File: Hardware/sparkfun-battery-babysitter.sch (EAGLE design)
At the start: 55 parts, among them U1 BQ24075, U2 BQ27441-G1

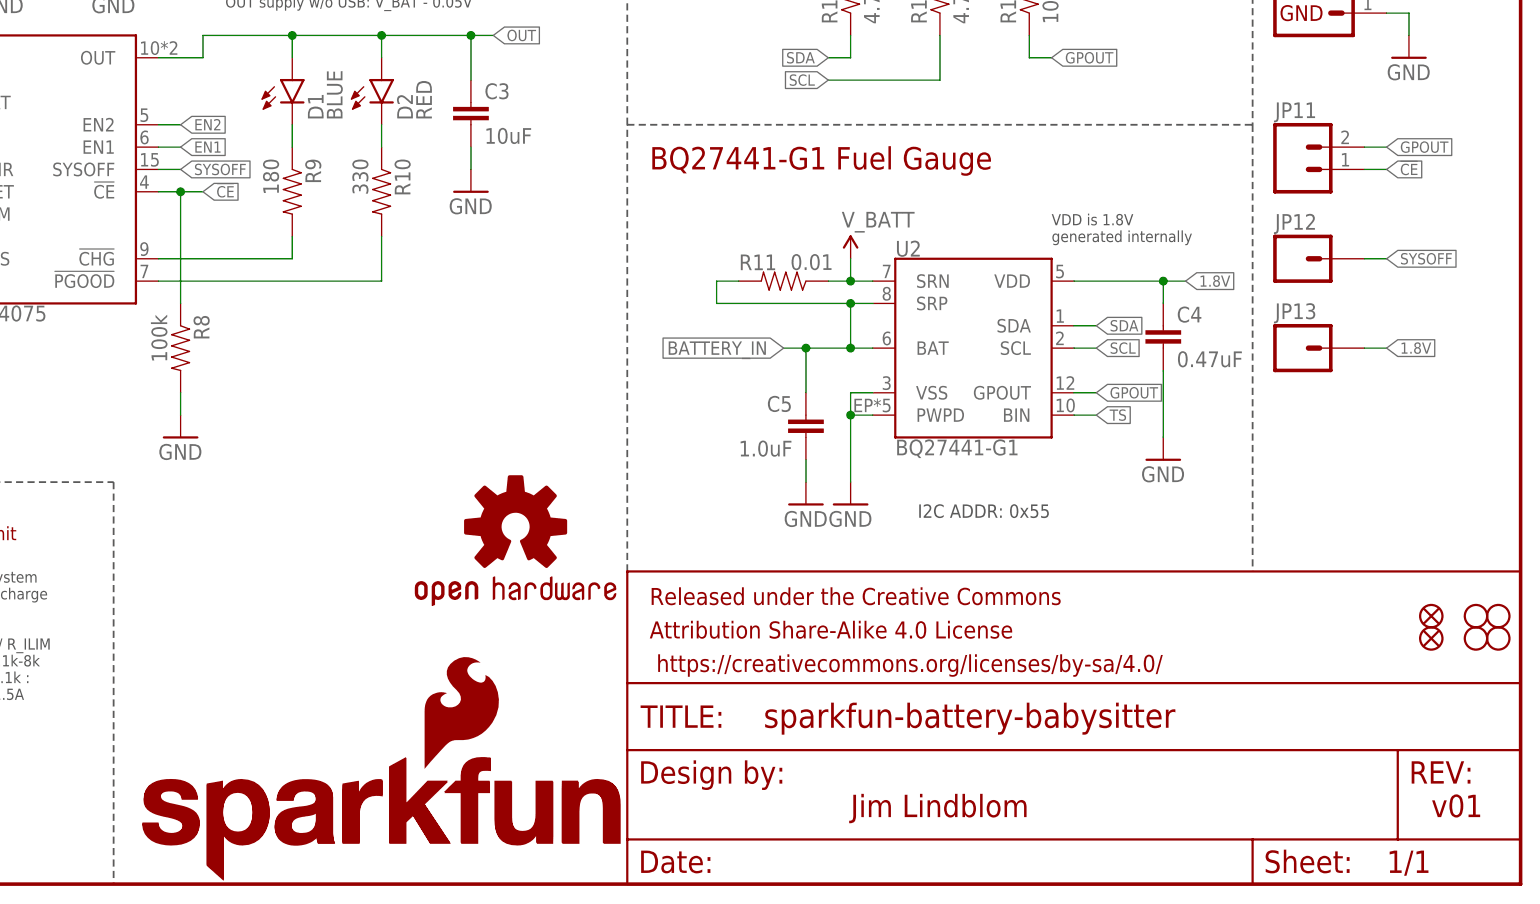
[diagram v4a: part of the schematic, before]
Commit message: Adding SJ5, to set power LED to PWR or PGOOD.
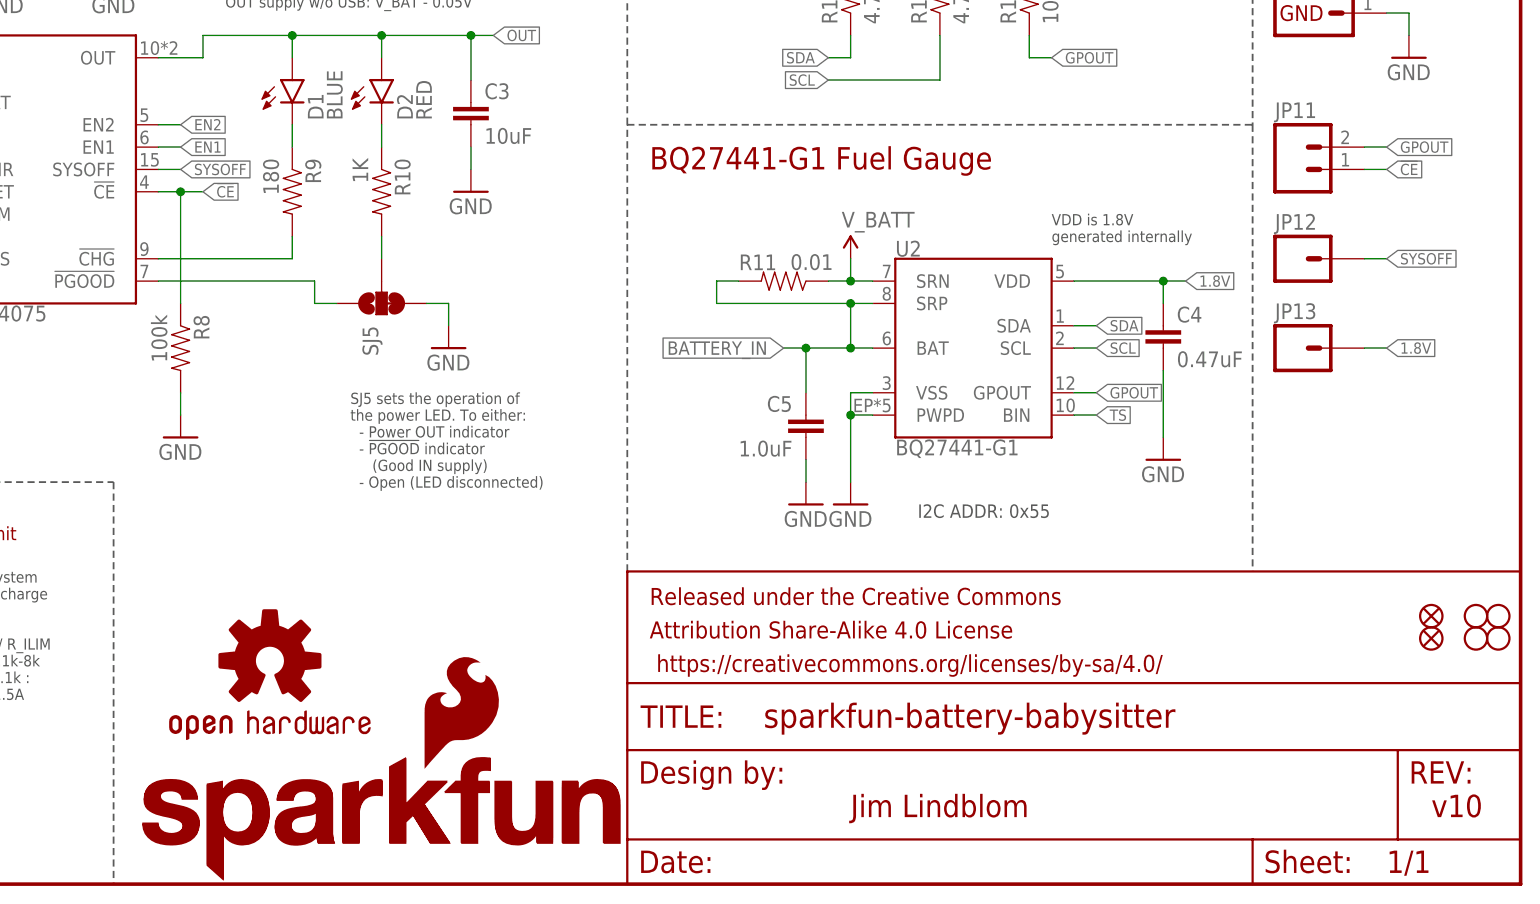
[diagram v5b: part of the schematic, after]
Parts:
- added SJ5: JUMPER-PAD-3-2OF3_NC_BY_TRACE_SMALL, SparkFun-Passives:JUMPER-PAD-3-2OF3_NC_BY_TRACE_SMALL
- R10: value 330 -> 1K; device SparkFun-Resistors:330OHM1/10W1%(0603) -> SparkFun-Resistors:1KOHM-1/10W-1%(0603)
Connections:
- new net N$5: R10.2, SJ5.2
- net !PGOOD!: now also SJ5.1; no longer R10.2
- net GND: now also SJ5.3
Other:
- note added: "SJ5 sets the operation of the power LED. To either: - Power OUT indicator - !PGOOD! indicator (Good IN supply) - Open (LED disconnected)"
- note added: "v10"
- note removed: "v01"
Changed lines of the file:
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@@
 <?xml version="1.0" encoding="utf-8"?>
 <!DOCTYPE eagle SYSTEM "eagle.dtd">
-<eagle version="7.1.0">
+<eagle version="7.5.0">
 <drawing>
 <settings>
@@
 <part name="D2" library="SparkFun-LED" deviceset="LED-RED" device="0603" value="RED"/>
 <part name="R9" library="SparkFun-Resistors" deviceset="180OHM1/10W1%(0603)" device="" value="180"/>
-<part name="R10" library="SparkFun-Resistors" deviceset="330OHM1/10W1%(0603)" device="" value="330"/>
+<part name="R10" library="SparkFun-Resistors" deviceset="1KOHM-1/10W-1%(0603)" device="" value="1K"/>
 <part name="C3" library="SparkFun-Capacitors" deviceset="10UF10V10%(0805)" device="" value="10uF"/>
 <part name="GND15" library="SparkFun-Aesthetics" deviceset="GND" device=""/>
@@
 <attribute name="PROD_ID" value="SWCH-13215"/>
 </part>
+<part name="GND24" library="SparkFun-Aesthetics" deviceset="GND" device=""/>
+<part name="SJ5" library="SparkFun-Passives" deviceset="JUMPER-PAD-3-2OF3_NC_BY_TRACE" device="_SMALL" value=""/>
 </parts>
 <sheets>
@@
 <text x="220.98" y="127" size="2.54" layer="94" align="top-left">Headers</text>
 <text x="172.72" y="10.16" size="2.54" layer="94" align="top-left">Jim Lindblom</text>
-<text x="238.76" y="10.16" size="2.54" layer="94" align="top-left">v01</text>
+<text x="238.76" y="10.16" size="2.54" layer="94" align="top-left">v10</text>
 <text x="149.86" y="152.4" size="1.27" layer="97">SYSOFF controls supply
 to the V_OUT pin.
@@
 OUT supply w/o USB: V_BAT - 0.05V</text>
 <text x="180.34" y="43.18" size="1.524" layer="97" align="top-left">I2C ADDR: 0x55</text>
+<text x="115.824" y="55.88" size="1.27" layer="97" align="top-left">SJ5 sets the operation of
+the power LED. To either:
+  - Power OUT indicator
+  - !PGOOD! indicator
+     (Good IN supply)
+  - Open (LED disconnected)</text>
 </plain>
 <instances>
@@
 <instance part="JP4" gate="G$1" x="43.18" y="147.32"/>
 <instance part="LOGO1" gate="G$1" x="90.17" y="0.508"/>
-<instance part="LOGO3" gate="G$1" x="134.62" y="40.64"/>
+<instance part="LOGO3" gate="G$1" x="106.68" y="25.4"/>
 <instance part="R12" gate="G$1" x="177.8" y="157.48" rot="R270"/>
 <instance part="JP11" gate="G$1" x="223.52" y="81.28"/>
@@
 <attribute name="PROD_ID" x="231.14" y="149.86" size="1.27" layer="96" rot="R270" display="off"/>
 </instance>
+<instance part="GND24" gate="1" x="127" y="60.96"/>
+<instance part="SJ5" gate="G$1" x="119.38" y="66.04" rot="MR270"/>
 </instances>
 <busses>
@@
 <wire x1="27.94" y1="66.04" x2="27.94" y2="68.58" width="0.1524" layer="91"/>
 </segment>
+<segment>
+<pinref part="GND24" gate="1" pin="GND"/>
+<wire x1="127" y1="63.5" x2="127" y2="66.04" width="0.1524" layer="91"/>
+<pinref part="SJ5" gate="G$1" pin="3"/>
+<wire x1="124.46" y1="66.04" x2="127" y2="66.04" width="0.1524" layer="91"/>
+</segment>
 </net>
 <net name="D+" class="0">
@@
 <segment>
 <pinref part="U1" gate="G$1" pin="!PGOOD!"/>
-<pinref part="R10" gate="G$1" pin="2"/>
-<wire x1="93.98" y1="68.58" x2="119.38" y2="68.58" width="0.1524" layer="91"/>
-<wire x1="119.38" y1="68.58" x2="119.38" y2="73.66" width="0.1524" layer="91"/>
+<wire x1="93.98" y1="68.58" x2="111.76" y2="68.58" width="0.1524" layer="91"/>
+<wire x1="111.76" y1="68.58" x2="111.76" y2="66.04" width="0.1524" layer="91"/>
+<pinref part="SJ5" gate="G$1" pin="1"/>
+<wire x1="111.76" y1="66.04" x2="114.3" y2="66.04" width="0.1524" layer="91"/>
 </segment>
 </net>
@@
 </segment>
 </net>
+<net name="N$5" class="0">
+<segment>
+<pinref part="R10" gate="G$1" pin="2"/>
+<wire x1="119.38" y1="71.12" x2="119.38" y2="73.66" width="0.1524" layer="91"/>
+<pinref part="SJ5" gate="G$1" pin="2"/>
+</segment>
+</net>
